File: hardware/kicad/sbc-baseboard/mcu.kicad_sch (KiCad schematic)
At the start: 41 parts, among them J16 SWD, J3 USB-C HID to target, SW201 RESET, U201 MK64FN1M0VLL12, U202 USBLC6-2SC6, Y201 32.768kHz

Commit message: Clock sources flow downward; USB pairs ordered as on the ESD array
Every crystal is now drawn by one helper: the two XTAL lanes run out past
the side's route channels to two columns 7.62 mm apart, drop at right
angles through the crystal lying across them, on into one load capacitor
each and a shared GND rail with one GND symbol, which also takes the
crystal's ground pins. The capacitors no longer hang off the lanes beside
the hub with the crystal somewhere else; nothing crosses.

Library v0.2.2: USB pairs are listed D- above D+, the order of the lines
through a USBLC6 array, so J3/U202 now sit on the K64's USB rows with
straight wires and the hub's upstream routes no longer cross; the hub's XTAL
pins move to the bottom of its left column so the clock cluster hangs under
everything else there, with clear rows around VBUS_DET.

All sheets: ERC 0, contacts 0, merges 0, layout 0; connectivity unchanged.

Co-Authored-By: Claude Fable 5.1 <noreply@anthropic.com>
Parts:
- C203: value 12p -> 1u
- C205: value 1u -> 12p
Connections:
- net K64_RESET_N: now also C203.1; no longer C205.1
- net at C204.1, Y201.1: now also U201.29 (EXTAL32); no longer U201.28 (XTAL32)
- new net: C205.1, U201.28 (XTAL32), Y201.2

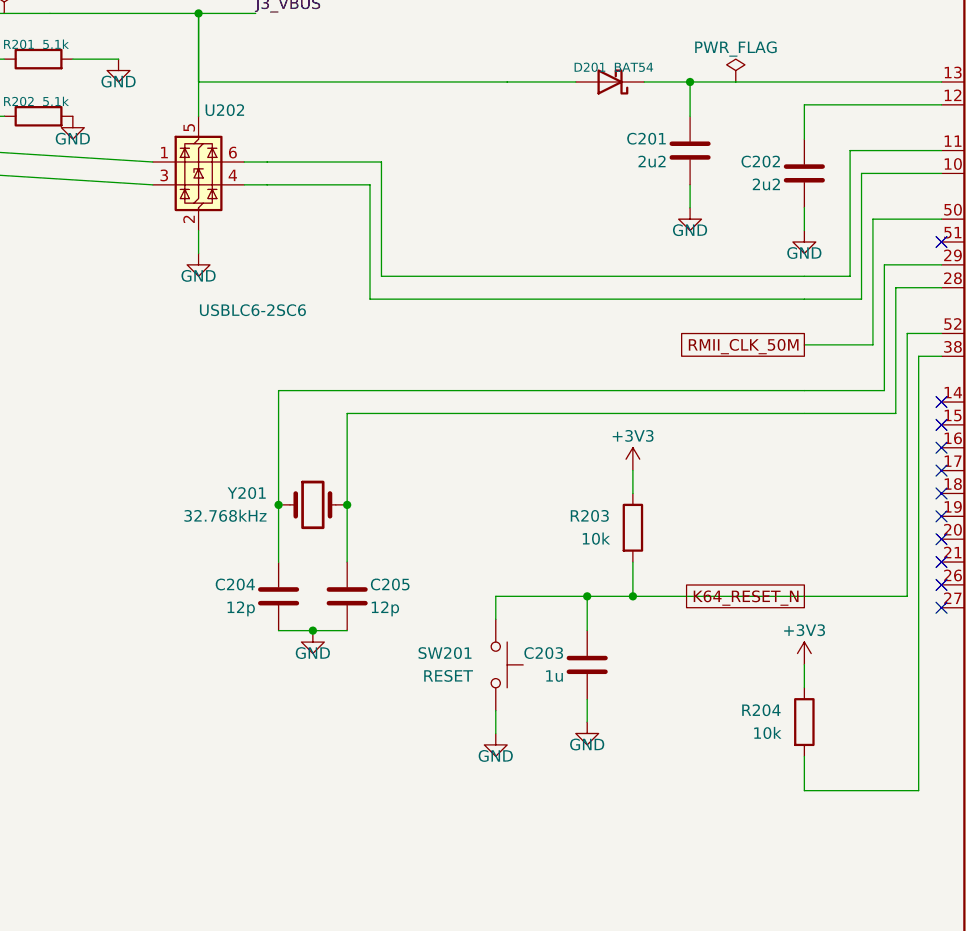
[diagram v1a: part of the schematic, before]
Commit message: Reset circuits flow downward: pull-up, capacitor and button in one cluster
A Reset attachment in the fan engine draws the network at the lane end, top to
bottom: rail symbol, pull-up, the node row where the lane arrives, the capacitor
straight below in the same column, one GND under it; a push button hangs from
the lane one column nearer the hub and shares the GND rail. It declares its
reaches, so the spread and slide passes keep the neighbouring rows clear. Used
for the K64 (RESET), the USB2517 and the K20 (DAP RESET); the K20's SWD header
takes the K20_RESET_N label instead of a fourth wire into the node. Netlist
membership unchanged (356 nets); ERC, geometry, connectivity and layout gates
all at zero.

Co-Authored-By: Claude Fable 5.1 <noreply@anthropic.com>
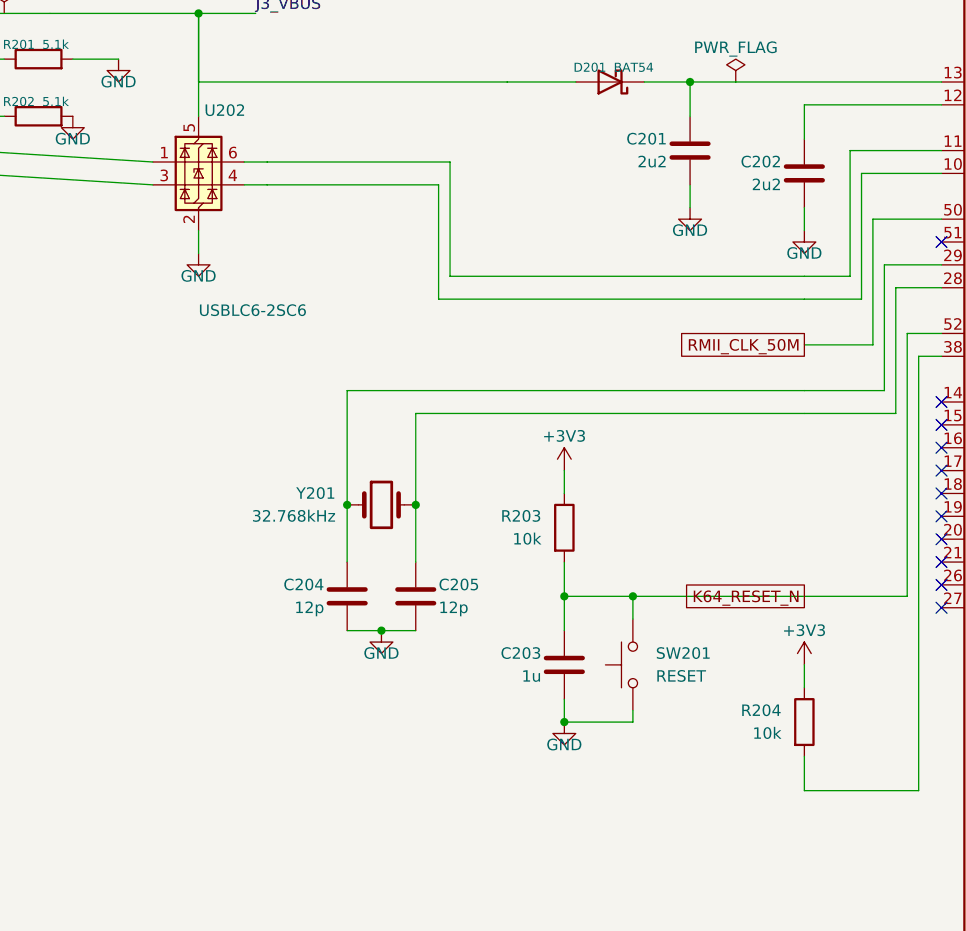
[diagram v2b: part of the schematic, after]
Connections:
- net GND: now also SW201.1; no longer SW201.2
- net K64_RESET_N: now also SW201.2; no longer SW201.1

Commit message: USB 2.0 differential pairs named for the router; USB net class; ports aligned
Every USB 2.0 data net is now <base>_P / <base>_N, the suffixes KiCad's PCB
editor pairs up: J1_D, J3_D, PORT1_D..PORT4_D on the receptacle side of each
ESD array; HUB_UP and HUB_DN1..HUB_DN7 at the hub; K64_USB and FTDI_USB at the
chips. All 15 pairs are complete with D+ on _P. The project file gains a USB
net class assigned by pattern (differential geometry to be set from the
stackup). The labels sit at wire ends with their text along the pair's own
wire; routes now run their last leg into a side pin as one wire so a label at
the pin end owns the stretch (Conn join=False keeps a shared stub where two
routes meet at one pin). The USB-A receptacles and their switches move down
1.27 mm so the pairs run straight from the ESD arrays, and the port ESD arrays
move left to make room for the labels. Netlist membership unchanged (356
nets); ERC, geometry, connectivity, layout and reproducibility gates all
clean.

Co-Authored-By: Claude Fable 5.1 <noreply@anthropic.com>
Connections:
- net K64_USB_P: now reaches U201.10 (USB0_DP), U202.4 (I/O2)
- net K64_USB_N: now reaches U201.11 (USB0_DM), U202.6 (I/O1)
- net J3_D_P: now reaches J3.A6 (D+), J3.B6 (D+), U202.3 (I/O2)
- net J3_D_N: now reaches J3.A7 (D-), J3.B7 (D-), U202.1 (I/O1)
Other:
- note added: "USB 2.0: K64_USB_P/N (K64 to U202) and J3_D_P/N (U202 to J3) are 90 ohm differential pairs, net class USB: route as pairs, no stubs."
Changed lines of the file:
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@@
 		)
 	)
+	(text "USB 2.0: K64_USB_P/N (K64 to U202) and J3_D_P/N (U202 to J3) are 90 ohm differential pairs, net class USB: route as pairs, no stubs."
+		(exclude_from_sim no)
+		(at 16 30.5 0)
+		(effects
+			(font
+				(size 1.5 1.5)
+			)
+			(justify left bottom)
+		)
+	)
 	(symbol
 		(lib_id "calico-ic:MK64FN1M0VLL12")
@@
 		(pts
 			(xy 50.8 76.2)
-			(xy 58.42 76.2)
+			(xy 60.96 76.2)
 		)
 		(stroke
@@
 		(pts
 			(xy 50.8 78.74)
-			(xy 58.42 78.74)
+			(xy 60.96 78.74)
 		)
 		(stroke
@@
 	(wire
 		(pts
-			(xy 58.42 76.2)
-			(xy 58.42 78.74)
+			(xy 60.96 76.2)
+			(xy 60.96 78.74)
 		)
 		(stroke
@@
 	)
 	(junction
-		(at 58.42 76.2)
+		(at 60.96 76.2)
 		(diameter 0)
 		(color 0 0 0 0)
@@
 		(pts
 			(xy 50.8 71.12)
-			(xy 58.42 71.12)
+			(xy 60.96 71.12)
 		)
 		(stroke
@@
 		(pts
 			(xy 50.8 73.66)
-			(xy 58.42 73.66)
+			(xy 60.96 73.66)
 		)
 		(stroke
@@
 	(wire
 		(pts
-			(xy 58.42 71.12)
-			(xy 58.42 73.66)
+			(xy 60.96 71.12)
+			(xy 60.96 73.66)
 		)
 		(stroke
@@
 	)
 	(junction
-		(at 58.42 71.12)
+		(at 60.96 71.12)
 		(diameter 0)
 		(color 0 0 0 0)
@@
 	(wire
 		(pts
-			(xy 58.42 73.66)
+			(xy 60.96 73.66)
 			(xy 78.74 74.93)
 		)
@@
 	)
 	(junction
-		(at 58.42 73.66)
+		(at 60.96 73.66)
 		(diameter 0)
 		(color 0 0 0 0)
@@
 	(wire
 		(pts
-			(xy 58.42 76.2)
+			(xy 60.96 76.2)
 			(xy 78.74 77.47)
 		)
@@
 	)
 	(junction
-		(at 58.42 76.2)
+		(at 60.96 76.2)
 		(diameter 0)
 		(color 0 0 0 0)
@@
 		)
 	)
+	(label "J3_D_N"
+		(at 50.8 73.66 0)
+		(fields_autoplaced yes)
+		(effects
+			(font
+				(size 1.27 1.27)
+			)
+			(justify left bottom)
+		)
+	)
+	(label "J3_D_P"
+		(at 50.8 78.74 0)
+		(fields_autoplaced yes)
+		(effects
+			(font
+				(size 1.27 1.27)
+			)
+			(justify left bottom)
+		)
+	)
 	(wire
 		(pts
@@
 		(pts
 			(xy 111.76 74.93)
-			(xy 91.44 74.93)
-		)
-		(stroke
-			(width 0)
-			(type default)
-		)
-	)
-	(wire
-		(pts
-			(xy 91.44 74.93)
 			(xy 88.9 74.93)
 		)
@@
 		(pts
 			(xy 110.49 77.47)
-			(xy 91.44 77.47)
-		)
-		(stroke
-			(width 0)
-			(type default)
-		)
-	)
-	(wire
-		(pts
-			(xy 91.44 77.47)
 			(xy 88.9 77.47)
 		)
@@
 		(pts
 			(xy 326.39 57.15)
-			(xy 344.17 57.15)
-		)
-		(stroke
-			(width 0)
-			(type default)
-		)
-	)
-	(wire
-		(pts
-			(xy 344.17 57.15)
 			(xy 346.71 57.15)
 		)
@@
 		(pts
 			(xy 327.66 59.69)
-			(xy 344.17 59.69)
-		)
-		(stroke
-			(width 0)
-			(type default)
-		)
-	)
-	(wire
-		(pts
-			(xy 344.17 59.69)
 			(xy 346.71 59.69)
 		)
@@
 		(pts
 			(xy 328.93 219.71)
-			(xy 347.98 219.71)
-		)
-		(stroke
-			(width 0)
-			(type default)
-		)
-	)
-	(wire
-		(pts
-			(xy 347.98 219.71)
 			(xy 350.52 219.71)
 		)
@@
 		(pts
 			(xy 330.2 224.79)
-			(xy 347.98 224.79)
-		)
-		(stroke
-			(width 0)
-			(type default)
-		)
-	)
-	(wire
-		(pts
-			(xy 347.98 224.79)
 			(xy 350.52 224.79)
 		)
@@
 		(pts
 			(xy 331.47 229.87)
-			(xy 347.98 229.87)
-		)
-		(stroke
-			(width 0)
-			(type default)
-		)
-	)
-	(wire
-		(pts
-			(xy 347.98 229.87)
 			(xy 350.52 229.87)
 		)
@@
 		)
 	)
+	(label "K64_USB_P"
+		(at 88.9 77.47 0)
+		(fields_autoplaced yes)
+		(effects
+			(font
+				(size 1.27 1.27)
+			)
+			(justify left bottom)
+		)
+	)
+	(label "K64_USB_N"
+		(at 88.9 74.93 0)
+		(fields_autoplaced yes)
+		(effects
+			(font
+				(size 1.27 1.27)
+			)
+			(justify left bottom)
+		)
+	)

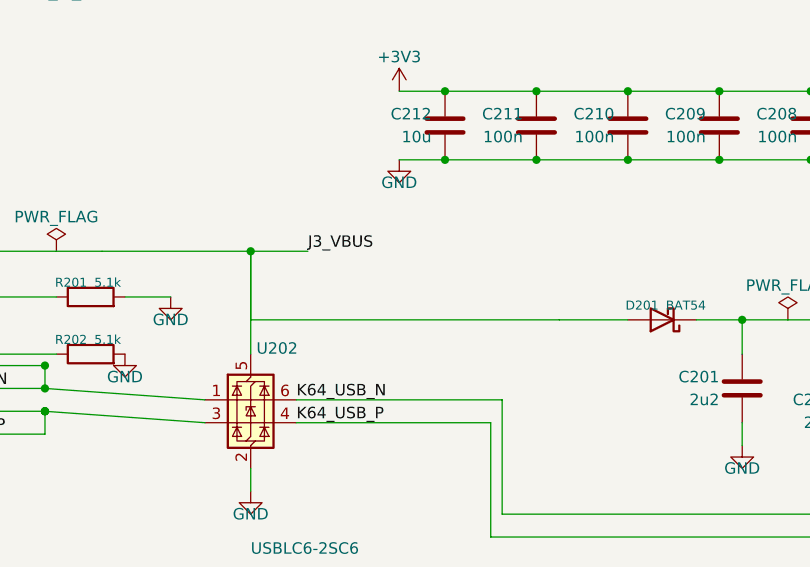
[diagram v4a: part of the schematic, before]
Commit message: Nothing drawn over anything else; FTDI Friend header; DAPLink per FRDM-K64F; 90 ohm USB class
Geometry gate now also reports two wires sharing a stretch, and is at zero on
every sheet. Routes into a stacked connector from one side take staggered
columns and rows; the signal relays are flipped so COM meets the header's
first pin without crossings; the opto-isolator moves above the passthrough
wires and taps the relay's COM lane; a tag before a route ends at the route's
target; routes into joined pins end at the join; the K64's VREGIN diode taps
the VBUS lane beside the ESD's stub; symbol mirrors are applied after
rotation, as KiCad does.

FT231X: the 3V3OUT lane stays on its pin row with its capacitor far out, clear
of the VCC decoupling; J9 mirrors the Adafruit FTDI Friend (VCC 5 V and pin 6
RTS by default on bridged solder jumpers; the first pass had left J9's VCC on
an open jumper only).

DAPLink K20, verified against DAPLink k20dx and the FRDM-K64F OpenSDA circuit:
PTC7 (SWDIO_IN) joins the SWDIO net, 33 R series resistors on the K20's USB
pair (K20_USB_P/N), notes and spec questions 12 and 14 resolved.

USB net class: 0.35 mm / 0.20 mm for 90 ohm on Advanced Circuits' standard
4-layer 62 mil stackup (spec section 8a). ERC 0, geometry 0, merges 0, layout
0, builds reproducible.

Co-Authored-By: Claude Fable 5.1 <noreply@anthropic.com>
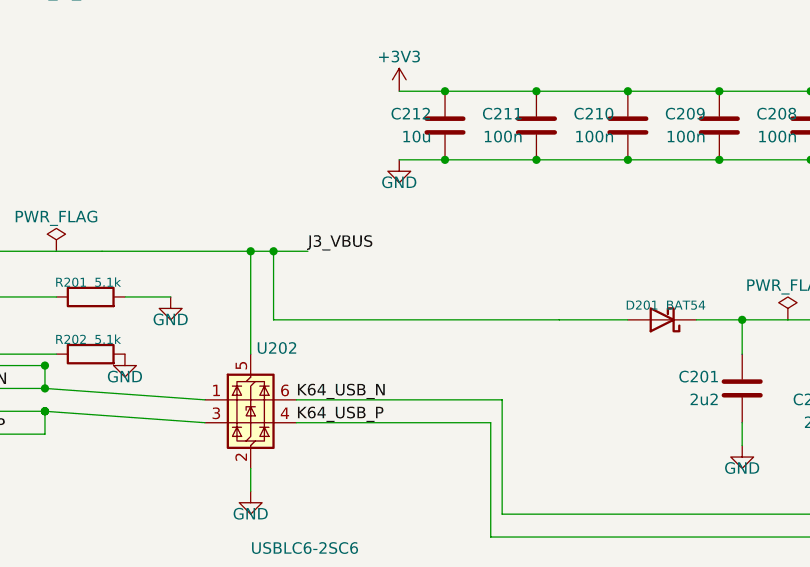
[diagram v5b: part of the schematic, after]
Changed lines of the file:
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@@
+		(color 0 0 0 0)
+	)
+	(junction
+		(at 86.36 58.42)
+		(diameter 0)
 		(color 0 0 0 0)
 	)
@@
 		(pts
 			(xy 118.11 66.04)
-			(xy 83.82 66.04)
-		)
-		(stroke
-			(width 0)
-			(type default)
-		)
-	)
-	(wire
-		(pts
-			(xy 83.82 66.04)
-			(xy 83.82 58.42)
-		)
-		(stroke
+			(xy 86.36 66.04)
+		)
+		(stroke
+			(width 0)
+			(type default)
+		)
+	)
+	(wire
+		(pts
+			(xy 86.36 66.04)
+			(xy 86.36 58.42)
+		)
+		(stroke

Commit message: Pairs laid as lanes, the rails as L3 regions, the Ethernet pairs named: the board ready for the bulk router
All sixteen USB 2.0 pair segments and the two Ethernet MDI pairs are laid
by the standard's placer from pair lanes in gen/layout.py: members at the
class geometry, escapes at the pads, the USB-C receptacles' doubled pads
bridged behind their rows, two pairs passing under the port pairs on the
bottom, every pair matched to within 0.25 mm, no crossings (the port
arrays and the J3 array use the house symbol drawn with I/O2 on top, the
K64's USB pins wired to its rows). J4 and J5 trade places so each stack's
pairs reach the hub row they are wired to. The ESD arrays, the series
parts and the SWD header are anchored for the lanes. The rails are
regions on In2.Cu at distinct priorities over a 3V3 base. The Ethernet
MDI pairs are named ETH_TD/RD and classed ETH (100 ohm). DRC: the 12
documented errors, no warnings but the unfilled rail islands; 499
connections for the bulk router (gen/pcb.py --route), which is running.

Co-Authored-By: Claude Fable 5.1 <noreply@anthropic.com>
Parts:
- U202: symbol Power_Protection:USBLC6-2SC6 -> calico-ic:USBLC6-2SC6-IO2up
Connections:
- net J3_D_N: now also U202.3 (I/O2); no longer U202.1 (I/O1)
- net J3_D_P: now also U202.1 (I/O1); no longer U202.3 (I/O2)
- net K64_USB_N: now also U202.4 (I/O2); no longer U202.6 (I/O1)
- net K64_USB_P: now also U202.6 (I/O1); no longer U202.4 (I/O2)
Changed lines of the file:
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@@
 	)
 	(symbol
-		(lib_id "Power_Protection:USBLC6-2SC6")
-		(at 83.82 74.93 0)
+		(lib_id "calico-ic:USBLC6-2SC6-IO2up")
+		(at 83.82 77.47 0)
 		(unit 1)
 		(body_style 1)
@@
 		(fields_autoplaced no)
 		(property "Reference" "U202"
-			(at 84.455 69.215 0)
+			(at 76.2 69.09 0)
 			(show_name no)
 			(do_not_autoplace no)
@@
 					(size 1.27 1.27)
 				)
-				(justify left)
+				(justify right)
 			)
 		)
 		(property "Footprint" "Package_TO_SOT_SMD:SOT-23-6"
-			(at 83.82 74.93 0)
+			(at 83.82 77.47 0)
 			(hide yes)
 			(show_name no)
@@
 		)
 		(property "Datasheet" "~"
-			(at 83.82 74.93 0)
+			(at 83.82 77.47 0)
 			(hide yes)
 			(show_name no)
@@
 			)
 		)
-		(property "Description" "Very low capacitance ESD protection diode, 2 data-line, SOT-23-6"
-			(at 83.82 74.93 0)
+		(property "Description" "USB 2.0 ESD protection array, two flow-through channels, SOT-23-6; drawn with I/O2 on the upper row"
+			(at 83.82 77.47 0)
 			(hide yes)
 			(show_name no)
@@
 			)
 		)
-		(pin "1"
-		)
-		(pin "2"
-		)
 		(pin "3"
 		)
+		(pin "1"
+		)
 		(pin "4"
 		)
+		(pin "6"
+		)
 		(pin "5"
 		)
-		(pin "6"
+		(pin "2"
 		)
 		(instances
@@
 		(pts
 			(xy 60.96 73.66)
-			(xy 78.74 74.93)
+			(xy 73.66 74.93)
 		)
 		(stroke
@@
 		(pts
 			(xy 60.96 76.2)
-			(xy 78.74 77.47)
+			(xy 73.66 77.47)
 		)
 		(stroke
@@
 		(pts
 			(xy 111.76 74.93)
-			(xy 88.9 74.93)
+			(xy 93.98 74.93)
 		)
 		(stroke
@@
 		(pts
 			(xy 110.49 77.47)
-			(xy 88.9 77.47)
+			(xy 93.98 77.47)
 		)
 		(stroke
@@
 	)
 	(label "K64_USB_P"
-		(at 88.9 77.47 0)
+		(at 93.98 77.47 0)
 		(fields_autoplaced yes)
 		(effects
@@
 	)
 	(label "K64_USB_N"
-		(at 88.9 74.93 0)
+		(at 93.98 74.93 0)
 		(fields_autoplaced yes)
 		(effects

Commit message: The three USB-C receptacles use the house GCT footprint with the peg holes clear of the outer ground pads: DRC at zero errors
gen/kit.py points USBC at calico:USB_C_Receptacle_GCT_USB4105-xx-A_16P_TopMnt_Horizontal_PegClear
(ecad-libraries 0.3.5, submodule bumped): KiCad's footprint rebuilt pad for pad
with A1, A12, B1 and B12 0.1 mm shorter at the peg end, hole to copper 0.29 mm
against the fab's 0.25 mm. Schematic rebuilt (ERC clean, the footprint field on
J1-J3, BOM, PDF), board regenerated with the placement unchanged; the twelve
hole-clearance errors are gone. README and the reference-design review record
the deviation from GCT's drawing.

Co-Authored-By: Claude Fable 5.1 <noreply@anthropic.com>
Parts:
- J3: footprint Connector_USB:USB_C_Receptacle_GCT_USB4105-xx-A_16P_TopMnt_Horizontal -> calico:USB_C_Receptacle_GCT_USB4105-xx-A_16P_TopMnt_Horizontal_PegClear
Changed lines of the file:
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@@
 			)
 		)
-		(property "Footprint" "Connector_USB:USB_C_Receptacle_GCT_USB4105-xx-A_16P_TopMnt_Horizontal"
+		(property "Footprint" "calico:USB_C_Receptacle_GCT_USB4105-xx-A_16P_TopMnt_Horizontal_PegClear"
 			(at 35.56 73.66 0)
 			(hide yes)
